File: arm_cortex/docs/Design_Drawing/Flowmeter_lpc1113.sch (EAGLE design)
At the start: 78 parts, among them IC2 OP07CN, IC5 OP07CN, U1 LPC1113FBD48/302,1, U2 LD1117S33CTR, U4 MAX232ACSE+, U5 MAX485CSA+, U6 7805TV, U7 MCP4921-E/P, U8 SP1490, X1 MKDSN1,5/3-5,08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

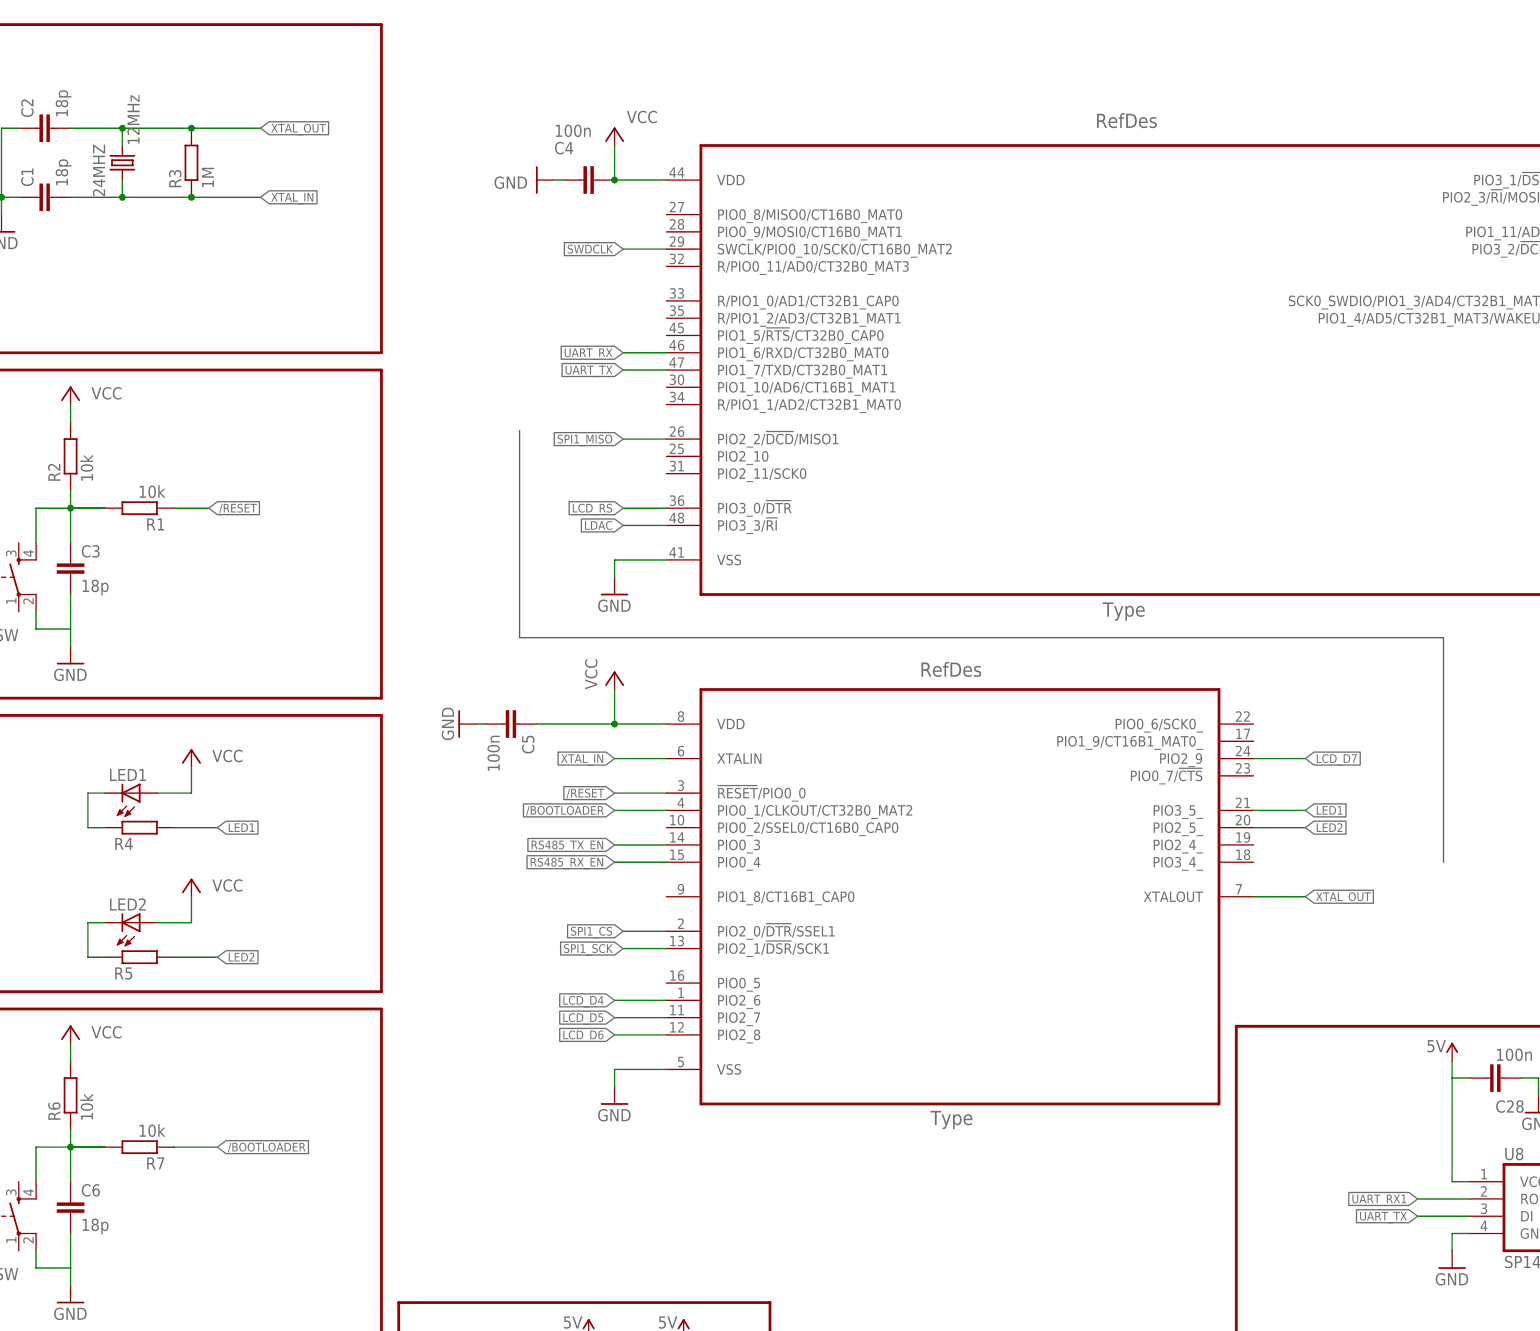
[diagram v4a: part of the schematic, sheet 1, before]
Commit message: 
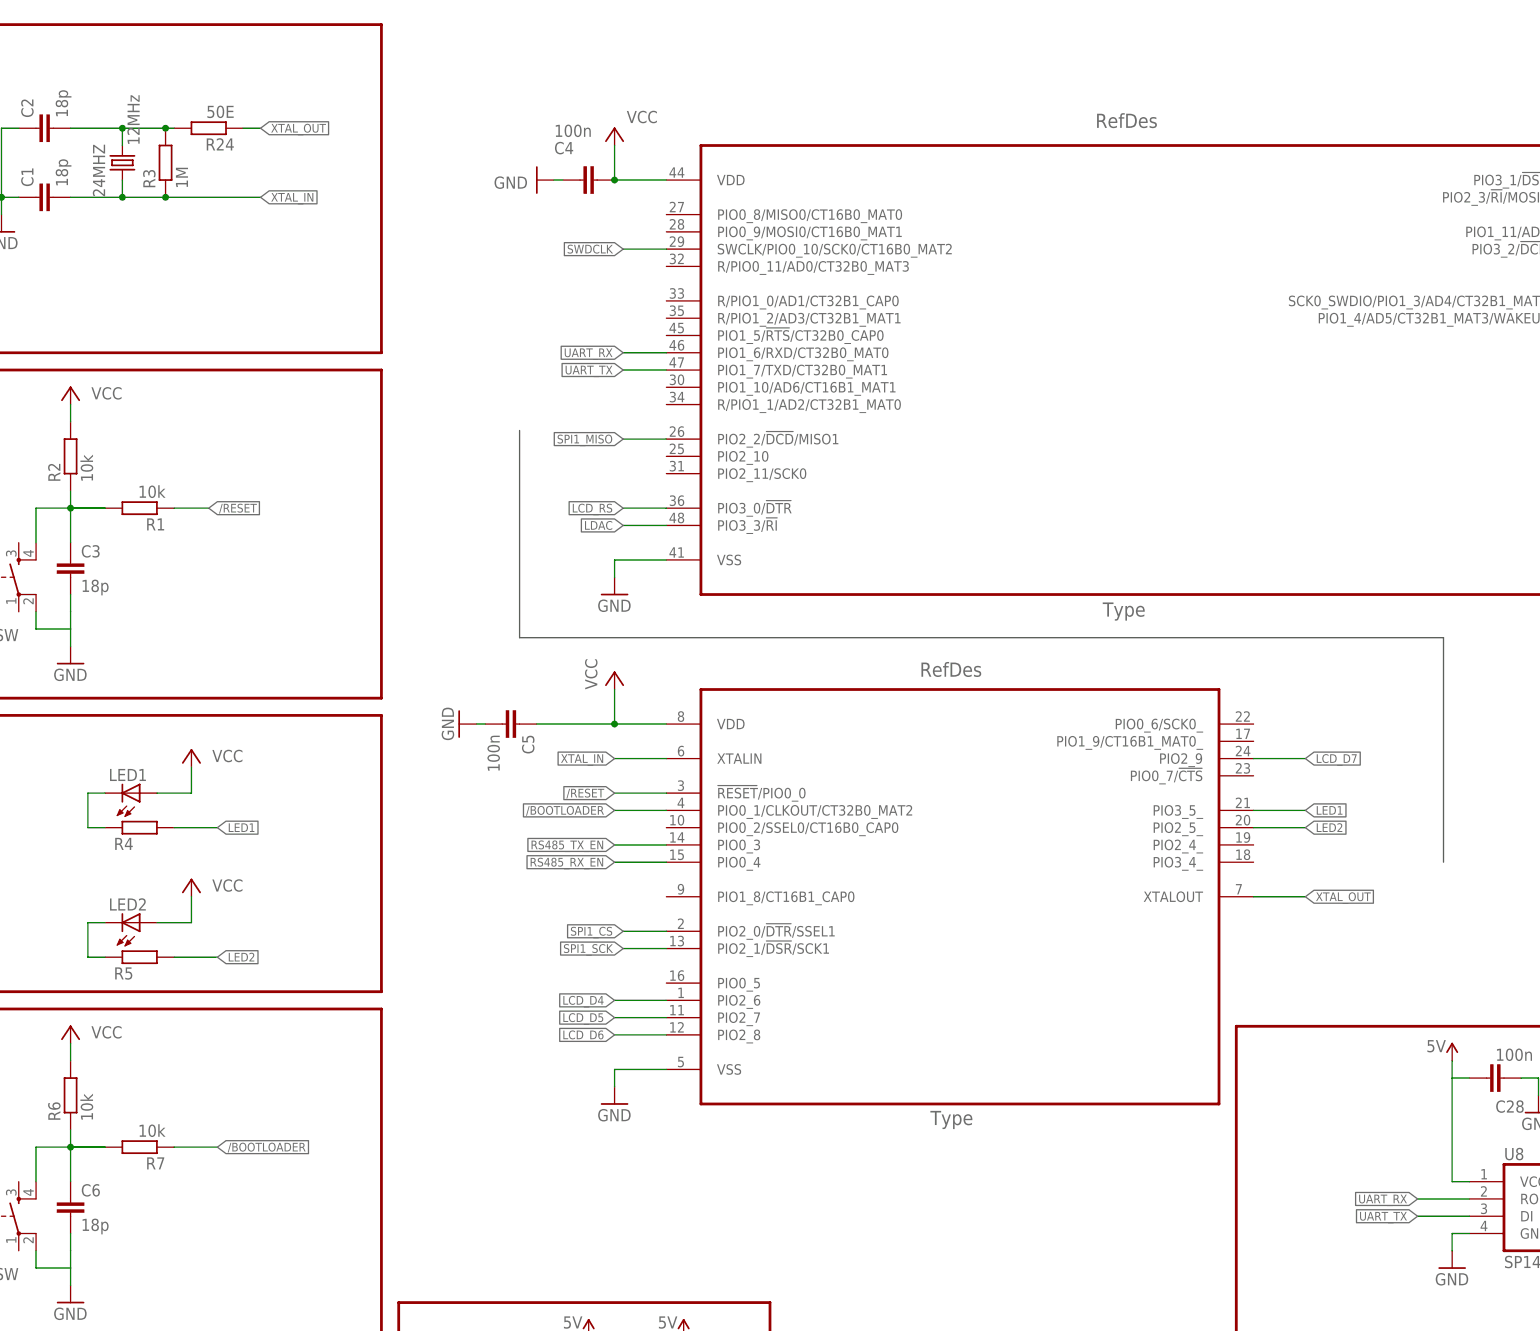
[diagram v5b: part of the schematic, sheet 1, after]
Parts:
- added R24: 50E, rcl:R-EU_R0805W
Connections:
- removed net UART_RX1: U8.RO
- new net N$6: 24MHZ.2, C2.2, R24.2, R3.2
- net UART_RX: now also U8.RO
- net XTAL_OUT: now also R24.1; no longer 24MHZ.2, C2.2, R3.2
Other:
- moved on the sheet: R3
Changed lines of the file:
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@@
 <setting verticaltext="up"/>
 </settings>
-<grid distance="0.05" unitdist="inch" unit="inch" style="lines" multiple="1" display="yes" altdistance="0.01" altunitdist="inch" altunit="inch"/>
+<grid distance="0.1" unitdist="inch" unit="inch" style="lines" multiple="1" display="no" altdistance="0.01" altunitdist="inch" altunit="inch"/>
 <layers>
 <layer number="1" name="Top" color="4" fill="1" visible="no" active="no"/>
@@
 <part name="R23" library="rcl" deviceset="R-EU_" device="R0805W" value="10k"/>
 <part name="3V9" library="supply1" deviceset="VCC" device=""/>
+<part name="R24" library="rcl" deviceset="R-EU_" device="R0805W" value="50E"/>
 </parts>
 <sheets>
@@
 <instance part="C2" gate="G$1" x="22.86" y="238.76" rot="R90"/>
 <instance part="C1" gate="G$1" x="22.86" y="228.6" rot="R90"/>
-<instance part="R3" gate="G$1" x="45.72" y="233.68" rot="R90"/>
+<instance part="R3" gate="G$1" x="41.91" y="233.68" rot="R90"/>
 <instance part="GND10" gate="1" x="17.78" y="223.52"/>
 <instance part="24MHZ" gate="G$1" x="35.56" y="233.68" smashed="yes" rot="R90">
@@
 <attribute name="VALUE" x="167.64" y="54.61" size="1.778" layer="96" rot="R180"/>
 </instance>
+<instance part="R24" gate="G$1" x="48.26" y="238.76" rot="R180"/>
 </instances>
 <busses>
@@
 <net name="XTAL_OUT" class="0">
 <segment>
-<wire x1="27.94" y1="238.76" x2="35.56" y2="238.76" width="0.1524" layer="91"/>
-<wire x1="35.56" y1="238.76" x2="45.72" y2="238.76" width="0.1524" layer="91"/>
-<wire x1="45.72" y1="238.76" x2="55.88" y2="238.76" width="0.1524" layer="91"/>
-<wire x1="35.56" y1="236.22" x2="35.56" y2="238.76" width="0.1524" layer="91"/>
-<junction x="45.72" y="238.76"/>
-<junction x="35.56" y="238.76"/>
-<label x="55.88" y="238.76" size="1.27" layer="95" xref="yes"/>
-<pinref part="C2" gate="G$1" pin="2"/>
-<pinref part="R3" gate="G$1" pin="2"/>
-<pinref part="24MHZ" gate="G$1" pin="2"/>
-</segment>
-<segment>
 <wire x1="201.93" y1="125.73" x2="209.55" y2="125.73" width="0.1524" layer="91"/>
 <label x="209.55" y="125.73" size="1.27" layer="95" xref="yes"/>
 <pinref part="U1" gate="A" pin="XTALOUT"/>
 </segment>
+<segment>
+<wire x1="53.34" y1="238.76" x2="55.88" y2="238.76" width="0.1524" layer="91"/>
+<pinref part="R24" gate="G$1" pin="1"/>
+<label x="55.88" y="238.76" size="1.27" layer="95" xref="yes"/>
+</segment>
 </net>
 <net name="XTAL_IN" class="0">
 <segment>
 <wire x1="27.94" y1="228.6" x2="35.56" y2="228.6" width="0.1524" layer="91"/>
-<wire x1="35.56" y1="228.6" x2="45.72" y2="228.6" width="0.1524" layer="91"/>
-<wire x1="45.72" y1="228.6" x2="55.88" y2="228.6" width="0.1524" layer="91"/>
+<wire x1="35.56" y1="228.6" x2="41.91" y2="228.6" width="0.1524" layer="91"/>
+<wire x1="41.91" y1="228.6" x2="55.88" y2="228.6" width="0.1524" layer="91"/>
 <wire x1="35.56" y1="231.14" x2="35.56" y2="228.6" width="0.1524" layer="91"/>
-<junction x="45.72" y="228.6"/>
+<junction x="41.91" y="228.6"/>
 <junction x="35.56" y="228.6"/>
 <label x="55.88" y="228.6" size="1.27" layer="95" xref="yes"/>
@@
 <pinref part="U1" gate="B" pin="PIO1_6/RXD/CT32B0_MAT0"/>
 </segment>
+<segment>
+<wire x1="226.06" y1="81.28" x2="233.68" y2="81.28" width="0.1524" layer="91"/>
+<label x="226.06" y="81.28" size="1.27" layer="95" rot="R180" xref="yes"/>
+<pinref part="U8" gate="G$1" pin="RO"/>
+</segment>
 </net>
 <net name="RS485_RX_EN" class="0">
@@
 </segment>
 </net>
-<net name="UART_RX1" class="0">
-<segment>
-<wire x1="226.06" y1="81.28" x2="233.68" y2="81.28" width="0.1524" layer="91"/>
-<label x="226.06" y="81.28" size="1.27" layer="95" rot="R180" xref="yes"/>
-<pinref part="U8" gate="G$1" pin="RO"/>
-</segment>
-</net>
 <net name="SWITCH0" class="0">
 <segment>
@@
 </segment>
 </net>
+<net name="N$6" class="0">
+<segment>
+<pinref part="R24" gate="G$1" pin="2"/>
+<pinref part="R3" gate="G$1" pin="2"/>
+<wire x1="43.18" y1="238.76" x2="41.91" y2="238.76" width="0.1524" layer="91"/>
+<pinref part="C2" gate="G$1" pin="2"/>
+<wire x1="27.94" y1="238.76" x2="35.56" y2="238.76" width="0.1524" layer="91"/>
+<junction x="41.91" y="238.76"/>
+<pinref part="24MHZ" gate="G$1" pin="2"/>
+<wire x1="35.56" y1="238.76" x2="41.91" y2="238.76" width="0.1524" layer="91"/>
+<wire x1="35.56" y1="236.22" x2="35.56" y2="238.76" width="0.1524" layer="91"/>
+<junction x="35.56" y="238.76"/>
+</segment>
+</net>
